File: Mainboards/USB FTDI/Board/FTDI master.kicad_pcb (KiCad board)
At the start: 2 copper layers, 67.4 x 54.3 mm, 52 parts, among them IC1 NCP1117ST, IC10 FT232RL, IC2 MCP1700T-1802E, IC3 CRE1S0505SC, IC4 IL0512S, IC5 IRF7416, IC7 ADuM142E0BRQZ-RL7, IC8 ADuM142E0BRQZ-RL7, IC9 ADuM142E0BRQZ-RL7, J1 USB_C_Receptacle_USB2.0, X2 AKL18X-04W, X3 IDC-Header_2x05_P2.54mm_Verti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, X4 ALLSERIALMASTERM

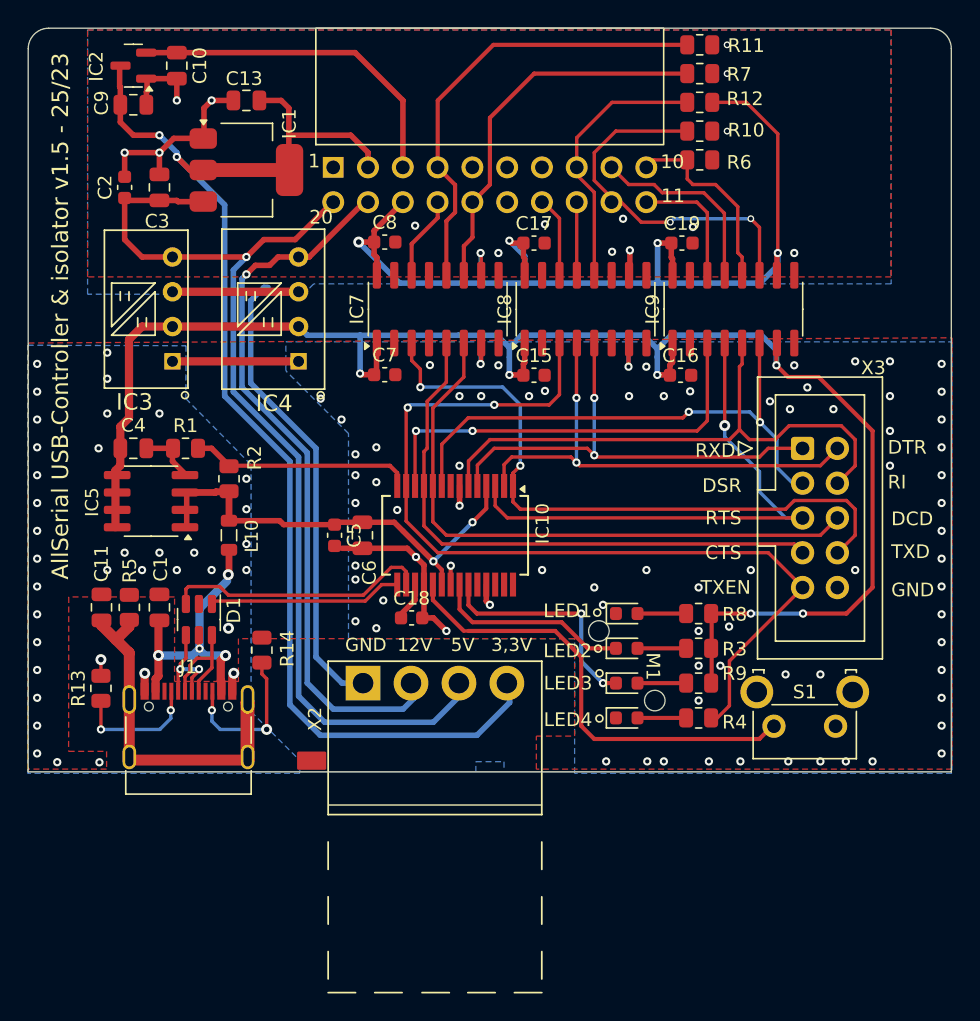
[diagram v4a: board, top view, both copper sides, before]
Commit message: Migrate to KiCad 9
Add eBus board
Add various libraries
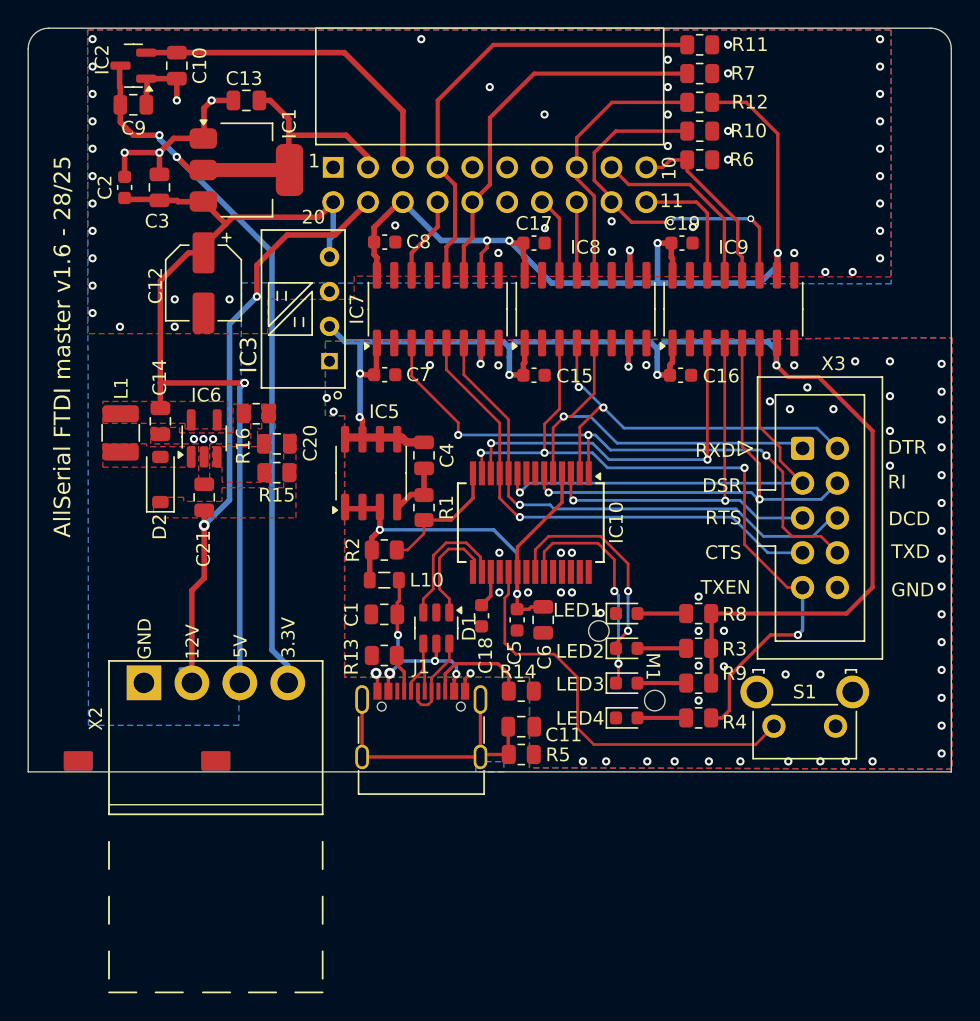
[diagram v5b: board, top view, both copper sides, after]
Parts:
- removed IC4: IL0512S, AllSerial:XPPOWER-ILxxxxS
- added C12: 100µ, Capacitor_SMD:CP_Elec_5x5.9, F.Cu at (127.6, 96.2)
- added C14: 4µ7, Capacitor_SMD:C_0805_2012Metric, F.Cu at (124.4, 106.3)
- added C20: 22pF, Capacitor_SMD:C_0805_2012Metric, F.Cu at (132.9, 108.0)
- added C21: 10µ, Capacitor_SMD:C_0805_2012Metric, F.Cu at (127.6, 111.8)
- added D2: MBR0530, Diode_SMD:D_SOD-123, F.Cu at (124.4, 110.5)
- added IC6: TPS61041, Package_TO_SOT_SMD:SOT-23-5_HandSoldering, F.Cu at (127.6, 107.5)
- added L1: 10µ, Inductor_SMD:L_1210_3225Metric, F.Cu at (121.5, 107.2)
- added R15: 300k, Resistor_SMD:R_0805_2012Metric, F.Cu at (132.9, 110.0)
- added R16: 33k, Resistor_SMD:R_0805_2012Metric, F.Cu at (131.4, 105.8)
- moved C11 31.9 mm to (150.8, 128.6), turned to 0 degrees
- moved R5 30.6 mm to (150.8, 130.6), turned to 180 degrees
- moved C4 21.2 mm to (143.7, 108.8), turned to -90 degrees
- moved R13 20.8 mm to (140.8, 123.4), turned to 180 degrees
- moved R14 19.2 mm to (150.8, 126.0), turned to 0 degrees
- moved R1 17.9 mm to (143.7, 112.6), turned to -90 degrees
- moved D1 17.3 mm to (144.6, 121.4)
- moved J1 17.0 mm to (143.5, 129.7)
- moved C1 16.4 mm to (140.8, 120.4), turned to 180 degrees
- moved IC5 16.2 mm to (139.8, 110.1), turned to 90 degrees
- moved X2 16.0 mm to (128.5, 125.4)
- moved C5 14.7 mm to (150.5, 120.8)
- moved C6 14.6 mm to (152.4, 120.8)
- moved R2 12.5 mm to (140.8, 115.7), turned to 0 degrees
- moved L10 11.8 mm to (140.8, 117.9), turned to 180 degrees
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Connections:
- net /RXDA renamed /Interface/RXD
- net /RXDB renamed /Interface/RXDB
- net /TXENA renamed /Interface/TXEN
- net /TXENB renamed /Interface/TXENB
- net /USB+ renamed /USB_P
- net /USB- renamed /USB_N
- net Net-(IC10-CBUS4) renamed /Interface/GPIO
- net Net-(IC10-TXD) renamed /Interface/TXD
- net Net-(IC10-~{CTS}) renamed /Interface/CTS
- net Net-(IC10-~{DCD}) renamed /Interface/DCD
- net Net-(IC10-~{DSR}) renamed /Interface/DSR
- net Net-(IC10-~{DTR}) renamed /Interface/DTR
- net Net-(IC10-~{RI}) renamed /Interface/RI
- net Net-(IC10-~{RTS}) renamed /Interface/RTS
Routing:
- net GND1: track 62.9 -> 19.6 mm, vias 14 -> 51
- net GND: track 29.9 -> 2.83 mm, vias 114 -> 58
- net +5V: track 131.2 -> 109.0 mm, vias 8 -> 7
- net +3V3_1: track 95.2 -> 73.5 mm
- net /Interface/TXEN: track 67.1 -> 54.8 mm, vias 2 -> 4
- net /USB_N: track 19.2 -> 9.85 mm
- net /Interface/RTS: track 40.2 -> 31.0 mm, vias 1 -> 2
- net Vio: track 79.6 -> 70.4 mm, vias 6 -> 5
- net +5V_1: track 74.9 -> 66.5 mm, vias 1 -> 2
- net /Interface/RI: track 42.2 -> 35.2 mm, vias 0 -> 2
- net /~{PWEN}: track 16.2 -> 9.49 mm
- net Net-(J1-CC1): track 9.30 -> 2.83 mm, vias 2 -> 0
- net /Interface/DCD: track 44.5 -> 38.4 mm, vias 0 -> 1
- net /Interface/DTR: track 35.7 -> 29.7 mm
- net Net-(D1-VBUS): track 21.8 -> 16.0 mm
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- added copper zone on F.Cu, net +12V_1
- added copper zone on F.Cu, net +5V_1
- added copper zone on F.Cu, net Net-(D2-A)
- added copper zone on F.Cu, net Net-(IC6-FB)
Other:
- board text added: "${TITLE} ${REVISION} - ${ISSUE_DATE}"
- board text added: "3.3V"
- board text removed: "3,3V"
- board text removed: "AllSerial USB-Controller & isolator v1.5 - 25/23"

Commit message: Improve libraries
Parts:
- moved X2 1.40 mm to (128.5, 124.0)
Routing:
- net +12V_1: track 49.8 -> 43.5 mm
- net +5V_1: track 66.5 -> 63.7 mm
- net +3V3_1: track 73.5 -> 72.2 mm
- net /Interface/DSR: track 33.9 -> 35.1 mm
- net /Interface/RI: track 35.2 -> 36.0 mm

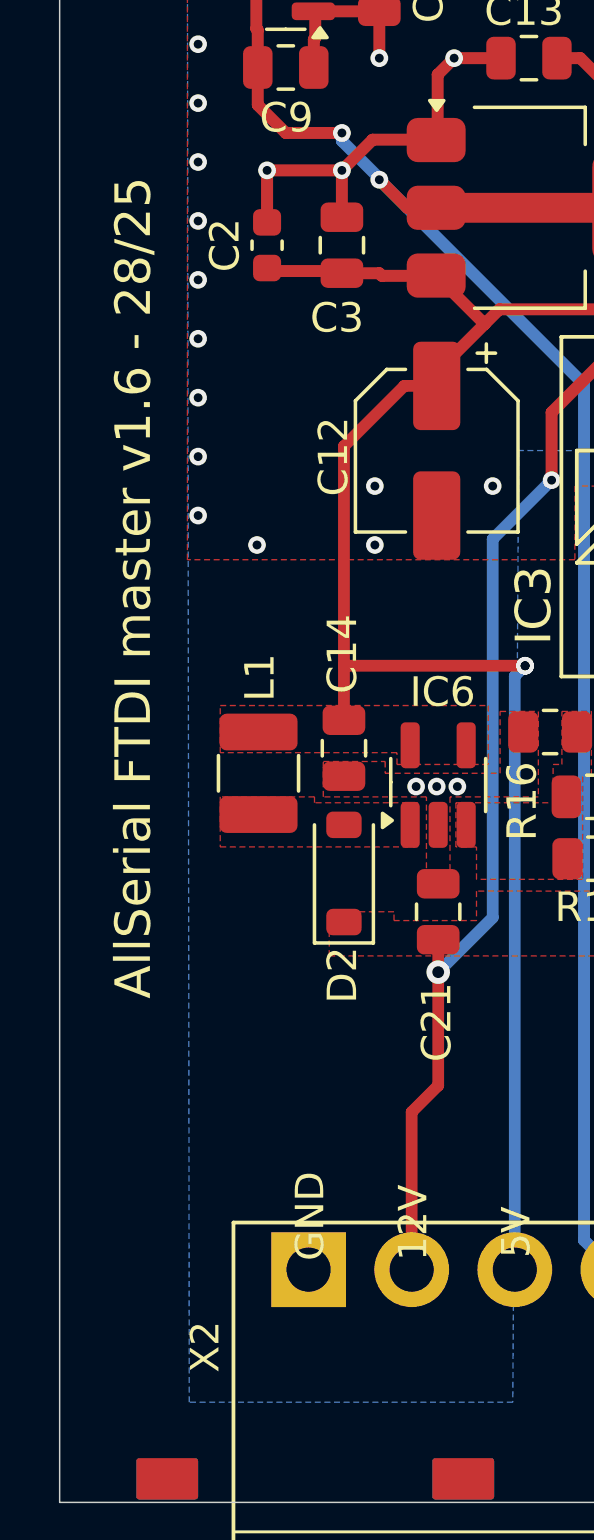
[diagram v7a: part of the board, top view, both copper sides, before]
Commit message: Remove pads from cutouts
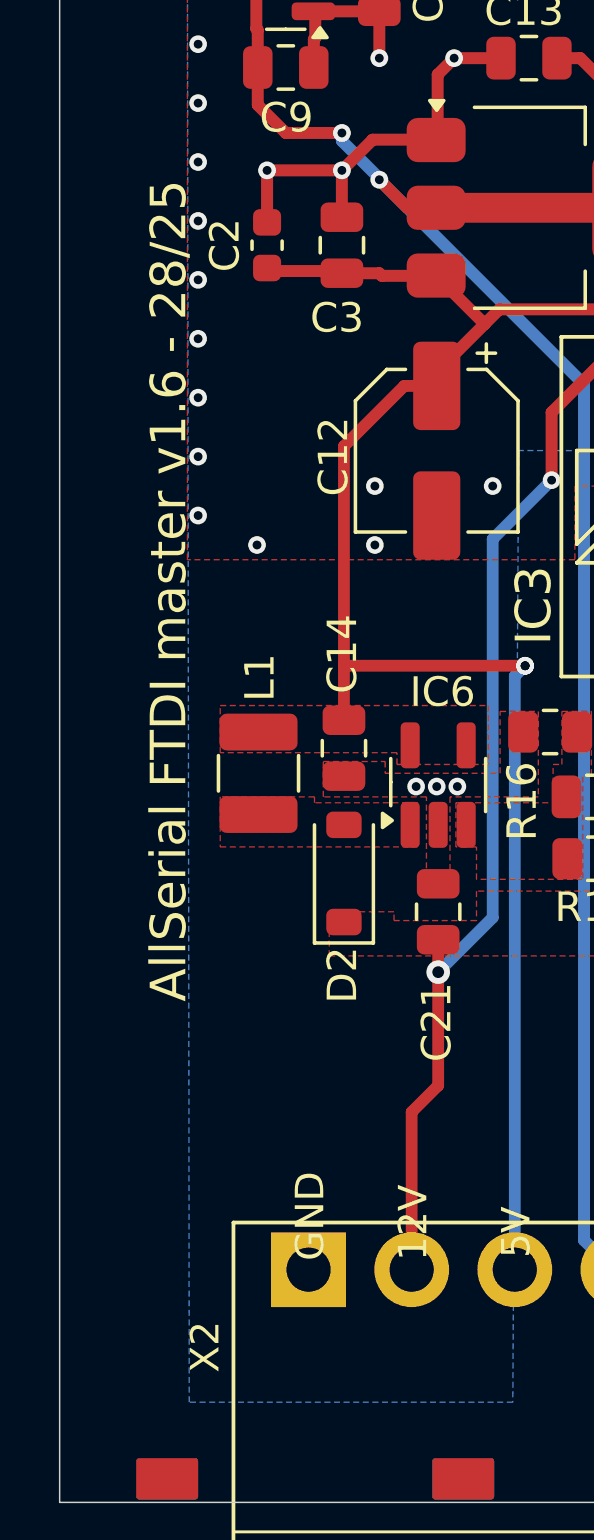
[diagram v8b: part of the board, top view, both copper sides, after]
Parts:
- R10, R11, R12, R6, R7: value 10k -> 22k
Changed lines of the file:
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@@
 			)
 		)
-		(property "Value" "10k"
+		(property "Value" "22k"
 			(at 0 1.65 180)
 			(layer "F.Fab")
@@
 			)
 		)
-		(property "LCSC" "C17414"
+		(property "LCSC" ""
 			(at 0 0 180)
 			(unlocked yes)
@@
 			)
 		)
-		(property "Value" "10k"
+		(property "Value" "22k"
 			(at 0 1.65 180)
 			(layer "F.Fab")
@@
 			)
 		)
-		(property "LCSC" "C17414"
+		(property "LCSC" ""
 			(at 0 0 180)
 			(unlocked yes)
@@
 			)
 		)
-		(property "Value" "10k"
+		(property "Value" "22k"
 			(at 0 1.65 180)
 			(layer "F.Fab")
@@
 			)
 		)
-		(property "LCSC" "C17414"
+		(property "LCSC" ""
 			(at 0 0 180)
 			(unlocked yes)
@@
 			)
 		)
-		(property "Value" "10k"
+		(property "Value" "22k"
 			(at 0 1.65 0)
 			(layer "F.Fab")
@@
 			)
 		)
-		(property "LCSC" "C17414"
+		(property "LCSC" ""
 			(at 0 0 0)
 			(unlocked yes)
@@
 			)
 		)
-		(property "Value" "10k"
+		(property "Value" "22k"
 			(at 0 1.65 180)
 			(layer "F.Fab")
@@
 			)
 		)
-		(property "LCSC" "C17414"
+		(property "LCSC" ""
 			(at 0 0 180)
 			(unlocked yes)
@@
 	)
 	(gr_text "${TITLE} ${REVISION} - ${ISSUE_DATE}"
-		(at 116.59 86.9 90)
+		(at 117.79 87 90)
 		(layer "F.SilkS")
 		(effects
